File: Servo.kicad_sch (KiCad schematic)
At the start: 28 parts, among them J10 Conn_01x03_Pin, J11 Conn_01x03_Pin, J12 Conn_01x03_Pin, J13 Conn_01x03_Pin, J14 Conn_01x03_Pin, J15 Conn_01x03_Pin, J2 Conn_01x03_Pin, J3 Conn_01x03_Pin, J4 Conn_01x03_Pin, J5 Conn_01x03_Pin, J6 Conn_01x03_Pin, J7 Conn_01x03_Pin, J8 Conn_01x03_Pin, J9 Conn_01x03_Pin

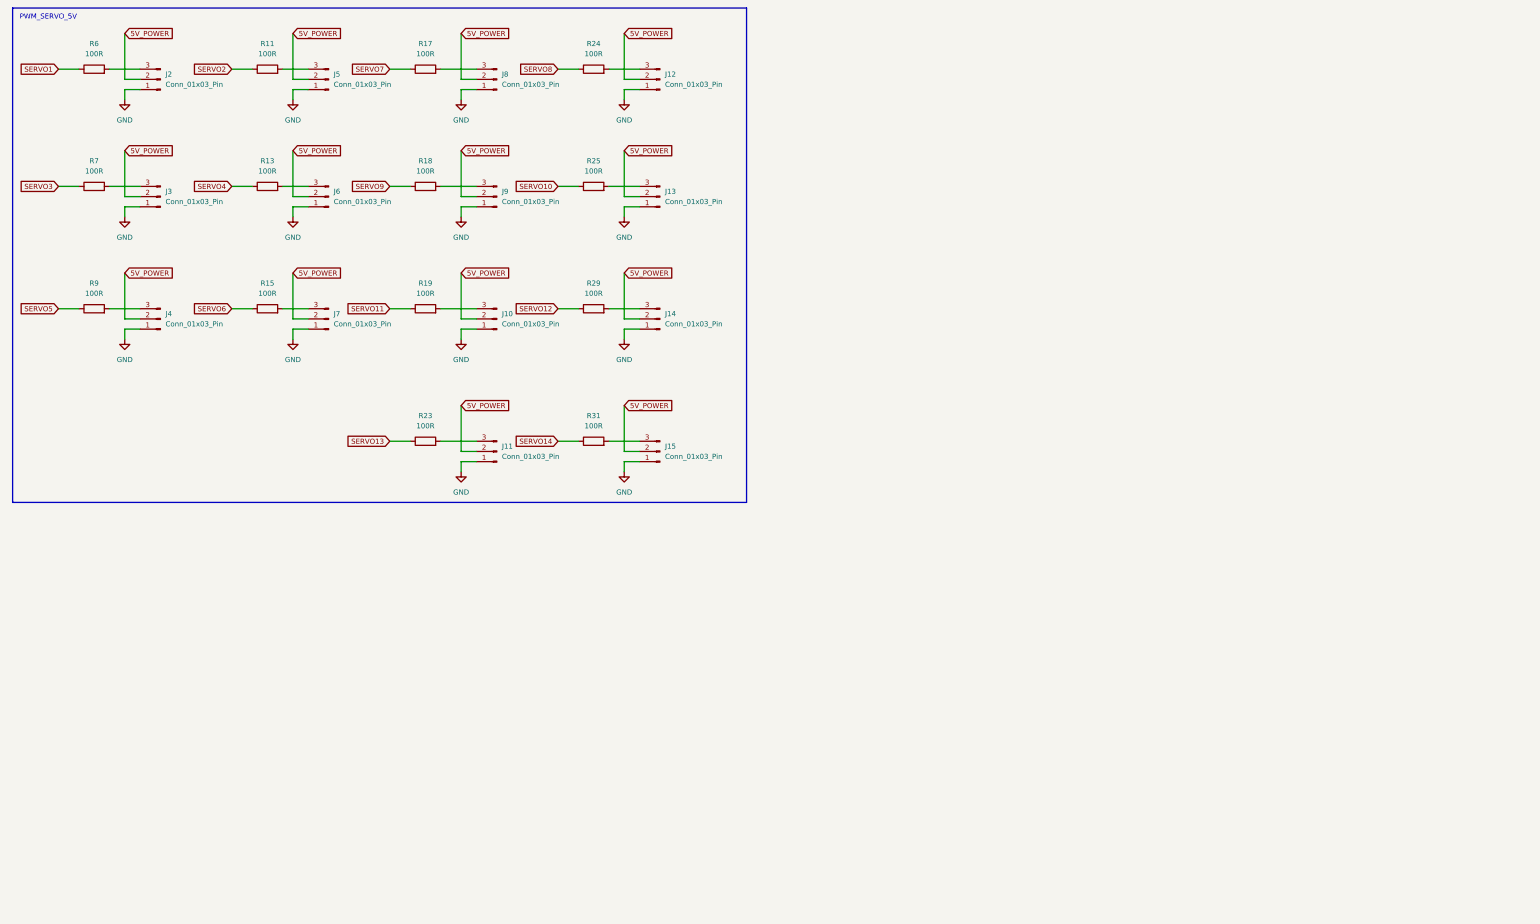
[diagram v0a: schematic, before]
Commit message: update servo output
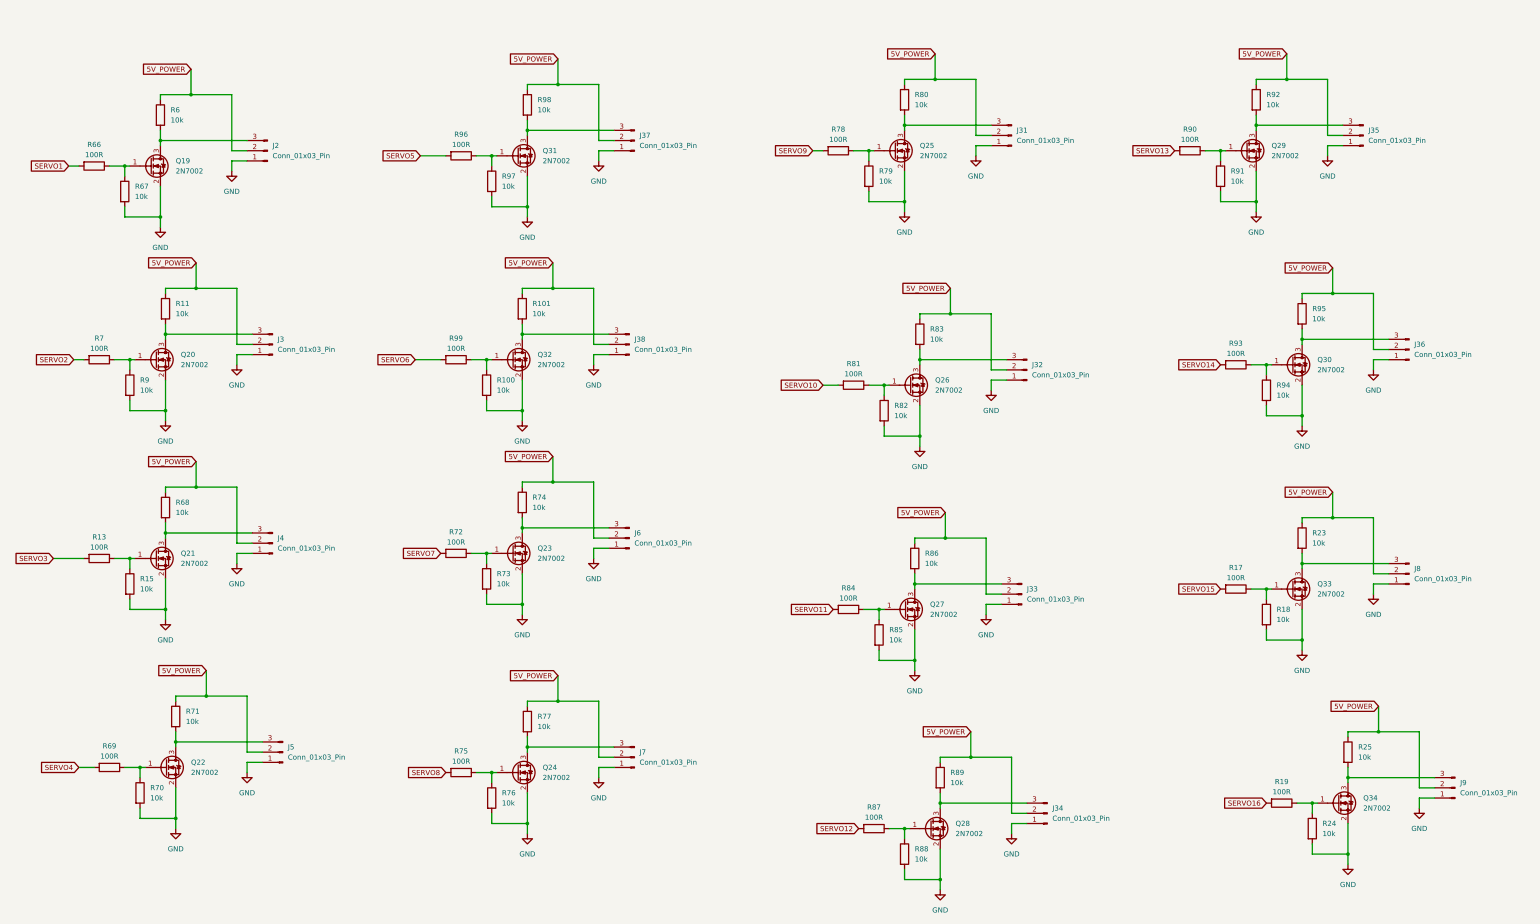
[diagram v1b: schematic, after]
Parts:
- removed J10, J11, J12, J13, J14, J15: Conn_01x03_Pin, symbol Connector:Conn_01x03_Pin
- removed R29, R31: 100R, symbol Device:R
- added J31, J32, J33, J34, J35, J36, J37, J38: Conn_01x03_Pin, Connector_JST:JST_XH_B3B-XH-AM_1x03_P2.50mm_Vertical, symbol Connector:Conn_01x03_Pin
- added Q19, Q20, Q21, Q22, Q23, Q24, Q25, Q26, Q27, Q28, Q29, Q30, Q31, Q32, Q33, Q34: 2N7002, Package_TO_SOT_SMD:SOT-23, symbol Transistor_FET:2N7002
- added R100, R101, R67, R68, R70, R71, R73, R74, R76, R77, R79, R80, R82, R83, R85, R86, R88, R89, R91, R92, R94, R95, R97, R98: 10k, Resistor_SMD:R_0201_0603Metric_Pad0.64x0.40mm_HandSolder, symbol Device:R
- added R66, R69, R72, R75, R78, R81, R84, R87, R90, R93, R96, R99: 100R, Resistor_SMD:R_0201_0603Metric_Pad0.64x0.40mm_HandSolder, symbol Device:R
- J2, J3, J4, J5, J6, J7, J8, J9: footprint (none) -> Connector_JST:JST_XH_B3B-XH-AM_1x03_P2.50mm_Vertical
- R11, R15, R18, R23, R24, R25, R6, R9: value 100R -> 10k; footprint (none) -> Resistor_SMD:R_0201_0603Metric_Pad0.64x0.40mm_HandSolder
- R13, R17, R19, R7: footprint (none) -> Resistor_SMD:R_0201_0603Metric_Pad0.64x0.40mm_HandSolder
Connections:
- net 5V_POWER: now also R11.1, R23.1, R25.1, R6.1, J31.2 (Pin_2), J32.2 (Pin_2), J33.2 (Pin_2), J34.2 (Pin_2), J35.2 (Pin_2), J36.2 (Pin_2), J37.2 (Pin_2), J38.2 (Pin_2), R101.1, R68.1, R71.1, R74.1, R77.1, R80.1, R83.1, R86.1, R89.1, R92.1, R95.1, R98.1
- net GND: now also R15.2, R18.2, R24.2, R9.2, J31.1 (Pin_1), J32.1 (Pin_1), J33.1 (Pin_1), J34.1 (Pin_1), J35.1 (Pin_1), J36.1 (Pin_1), J37.1 (Pin_1), J38.1 (Pin_1), Q19.2 (S), Q20.2 (S), Q21.2 (S), Q22.2 (S), Q23.2 (S), Q24.2 (S), Q25.2 (S), Q26.2 (S), Q27.2 (S), Q28.2 (S), Q29.2 (S), Q30.2 (S), Q31.2 (S), Q32.2 (S), Q33.2 (S), Q34.2 (S), R100.2, R67.2, R70.2, R73.2, R76.2, R79.2, R82.2, R85.2, R88.2, R91.2, R94.2, R97.2
- net SERVO1: now also R66.2; no longer R6.1
- net SERVO10: now also R81.2; no longer R25.1
- net SERVO11: now also R84.2; no longer R19.1
- net SERVO12: now also R87.2
- net SERVO13: now also R90.2; no longer R23.1
- net SERVO14: now also R93.2
- net SERVO2: now also R7.2; no longer R11.1
- net SERVO3: now also R13.2; no longer R7.1
- net SERVO4: now also R69.2; no longer R13.1
- net SERVO5: now also R96.2; no longer R9.1
- net SERVO6: now also R99.2; no longer R15.1
- net SERVO7: now also R72.2; no longer R17.1
- net SERVO8: now also R75.2; no longer R24.1
- net SERVO9: now also R78.2; no longer R18.1
- net at J9.3 (Pin_3): now also R25.2, Q34.3 (D); no longer R18.2
- net at J7.3 (Pin_3): now also Q24.3 (D), R77.2; no longer R15.2
- net at J3.3 (Pin_3): now also R11.2, Q20.3 (D); no longer R7.2
- net at J8.3 (Pin_3): now also R23.2, Q33.3 (D); no longer R17.2
- net at J6.3 (Pin_3): now also Q23.3 (D), R74.2; no longer R13.2
- net at J5.3 (Pin_3): now also Q22.3 (D), R71.2; no longer R11.2
- net at J2.3 (Pin_3), R6.2: now also Q19.3 (D)
- net at J4.3 (Pin_3): now also Q21.3 (D), R68.2; no longer R9.2
- net SERVO16: now reaches R19.2
- new net: Q20.1 (G), R7.1, R9.1
- new net: Q30.1 (G), R93.1, R94.1
- new net: J36.3 (Pin_3), Q30.3 (D), R95.2
- new net: Q26.1 (G), R81.1, R82.1
- new net: J32.3 (Pin_3), Q26.3 (D), R83.2
- new net: Q21.1 (G), R13.1, R15.1
- new net: Q33.1 (G), R17.1, R18.1
- new net: J33.3 (Pin_3), Q27.3 (D), R86.2
- new net: Q24.1 (G), R75.1, R76.1
- new net: Q23.1 (G), R72.1, R73.1
- new net: J34.3 (Pin_3), Q28.3 (D), R89.2
- new net: Q34.1 (G), R19.1, R24.1
- new net: Q25.1 (G), R78.1, R79.1
- new net: Q32.1 (G), R100.1, R99.1
- new net: Q19.1 (G), R66.1, R67.1
- new net: J35.3 (Pin_3), Q29.3 (D), R92.2
- new net: J31.3 (Pin_3), Q25.3 (D), R80.2
- new net: Q29.1 (G), R90.1, R91.1
- new net: Q31.1 (G), R96.1, R97.1
- new net: J37.3 (Pin_3), Q31.3 (D), R98.2
- new net: J38.3 (Pin_3), Q32.3 (D), R101.2
- new net: Q27.1 (G), R84.1, R85.1
- new net: Q22.1 (G), R69.1, R70.1
- new net: Q28.1 (G), R87.1, R88.1
- new net SERVO15: R17.2
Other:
- note removed: "PWM_SERVO_5V"
- moved on the sheet: J2

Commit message: v1 - need to change resistor package
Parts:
- R100, R101: footprint Resistor_SMD:R_0201_0603Metric_Pad0.64x0.40mm_HandSolder -> Capacitor_SMD:C_0402_1005Metric
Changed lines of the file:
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@@
 			)
 		)
-		(property "Footprint" "Resistor_SMD:R_0201_0603Metric_Pad0.64x0.40mm_HandSolder"
+		(property "Footprint" "Capacitor_SMD:C_0402_1005Metric"
 			(at 137.922 113.03 90)
 			(effects
@@
 			)
 		)
-		(property "Footprint" "Resistor_SMD:R_0201_0603Metric_Pad0.64x0.40mm_HandSolder"
+		(property "Footprint" "Capacitor_SMD:C_0402_1005Metric"
 			(at 146.812 93.98 90)
 			(effects

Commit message: fix resistor and add schematic in pdf
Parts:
- R11, R13, R15, R17, R18, R19, R23, R24, R25, R6, R66, R67, R68, R69, R7, R70, R71, R72, R73, R74, R75, R76, R77, R78, R79, R80, R81, R82, R83, R84, R85, R86, R87, R88, R89, R9, R90, R91, R92, R93, R94, R95, R96, R97, R98, R99: footprint Resistor_SMD:R_0201_0603Metric_Pad0.64x0.40mm_HandSolder -> Resistor_SMD:R_0402_1005Metric
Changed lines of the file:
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@@
 			)
 		)
-		(property "Footprint" "Resistor_SMD:R_0201_0603Metric_Pad0.64x0.40mm_HandSolder"
+		(property "Footprint" "Resistor_SMD:R_0402_1005Metric"
 			(at 49.022 113.03 90)
 			(effects
@@
 			)
 		)
-		(property "Footprint" "Resistor_SMD:R_0201_0603Metric_Pad0.64x0.40mm_HandSolder"
+		(property "Footprint" "Resistor_SMD:R_0402_1005Metric"
 			(at 245.872 100.33 90)
 			(effects
@@
 			)
 		)
-		(property "Footprint" "Resistor_SMD:R_0201_0603Metric_Pad0.64x0.40mm_HandSolder"
+		(property "Footprint" "Resistor_SMD:R_0402_1005Metric"
 			(at 43.18 154.432 90)
 			(effects
@@
 			)
 		)
-		(property "Footprint" "Resistor_SMD:R_0201_0603Metric_Pad0.64x0.40mm_HandSolder"
+		(property "Footprint" "Resistor_SMD:R_0402_1005Metric"
 			(at 332.232 170.18 90)
 			(effects
@@
 			)
 		)
-		(property "Footprint" "Resistor_SMD:R_0201_0603Metric_Pad0.64x0.40mm_HandSolder"
+		(property "Footprint" "Resistor_SMD:R_0402_1005Metric"
 			(at 139.192 215.9 90)
 			(effects
@@
 			)
 		)
-		(property "Footprint" "Resistor_SMD:R_0201_0603Metric_Pad0.64x0.40mm_HandSolder"
+		(property "Footprint" "Resistor_SMD:R_0402_1005Metric"
 			(at 133.35 207.772 90)
 			(effects
@@
 			)
 		)
-		(property "Footprint" "Resistor_SMD:R_0201_0603Metric_Pad0.64x0.40mm_HandSolder"
+		(property "Footprint" "Resistor_SMD:R_0402_1005Metric"
 			(at 49.022 162.56 90)
 			(effects
@@
 			)
 		)
-		(property "Footprint" "Resistor_SMD:R_0201_0603Metric_Pad0.64x0.40mm_HandSolder"
+		(property "Footprint" "Resistor_SMD:R_0402_1005Metric"
 			(at 250.952 210.82 90)
 			(effects
@@
 			)
 		)
-		(property "Footprint" "Resistor_SMD:R_0201_0603Metric_Pad0.64x0.40mm_HandSolder"
+		(property "Footprint" "Resistor_SMD:R_0402_1005Metric"
 			(at 148.082 196.85 90)
 			(effects
@@
 			)
 		)
-		(property "Footprint" "Resistor_SMD:R_0201_0603Metric_Pad0.64x0.40mm_HandSolder"
+		(property "Footprint" "Resistor_SMD:R_0402_1005Metric"
 			(at 326.39 106.172 90)
 			(effects
@@
 			)
 		)
-		(property "Footprint" "Resistor_SMD:R_0201_0603Metric_Pad0.64x0.40mm_HandSolder"
+		(property "Footprint" "Resistor_SMD:R_0402_1005Metric"
 			(at 227.33 52.832 90)
 			(effects
@@
 			)
 		)
-		(property "Footprint" "Resistor_SMD:R_0201_0603Metric_Pad0.64x0.40mm_HandSolder"
+		(property "Footprint" "Resistor_SMD:R_0402_1005Metric"
 			(at 341.122 151.13 90)
 			(effects
@@
 			)
 		)
-		(property "Footprint" "Resistor_SMD:R_0201_0603Metric_Pad0.64x0.40mm_HandSolder"
+		(property "Footprint" "Resistor_SMD:R_0402_1005Metric"
 			(at 47.752 64.77 90)
 			(effects
@@
 			)
 		)
-		(property "Footprint" "Resistor_SMD:R_0201_0603Metric_Pad0.64x0.40mm_HandSolder"
+		(property "Footprint" "Resistor_SMD:R_0402_1005Metric"
 			(at 329.692 41.91 90)
 			(effects
@@
 			)
 		)
-		(property "Footprint" "Resistor_SMD:R_0201_0603Metric_Pad0.64x0.40mm_HandSolder"
+		(property "Footprint" "Resistor_SMD:R_0402_1005Metric"
 			(at 56.642 45.72 90)
 			(effects
@@
 			)
 		)
-		(property "Footprint" "Resistor_SMD:R_0201_0603Metric_Pad0.64x0.40mm_HandSolder"
+		(property "Footprint" "Resistor_SMD:R_0402_1005Metric"
 			(at 146.812 142.24 90)
 			(effects
@@
 			)
 		)
-		(property "Footprint" "Resistor_SMD:R_0201_0603Metric_Pad0.64x0.40mm_HandSolder"
+		(property "Footprint" "Resistor_SMD:R_0402_1005Metric"
 			(at 242.062 41.91 90)
 			(effects
@@
 			)
 		)
-		(property "Footprint" "Resistor_SMD:R_0201_0603Metric_Pad0.64x0.40mm_HandSolder"
+		(property "Footprint" "Resistor_SMD:R_0402_1005Metric"
 			(at 57.912 93.98 90)
 			(effects
@@
 			)
 		)
-		(property "Footprint" "Resistor_SMD:R_0201_0603Metric_Pad0.64x0.40mm_HandSolder"
+		(property "Footprint" "Resistor_SMD:R_0402_1005Metric"
 			(at 314.96 52.832 90)
 			(effects
@@
 			)
 		)
-		(property "Footprint" "Resistor_SMD:R_0201_0603Metric_Pad0.64x0.40mm_HandSolder"
+		(property "Footprint" "Resistor_SMD:R_0402_1005Metric"
 			(at 233.172 60.96 90)
 			(effects
@@
 			)
 		)
-		(property "Footprint" "Resistor_SMD:R_0201_0603Metric_Pad0.64x0.40mm_HandSolder"
+		(property "Footprint" "Resistor_SMD:R_0402_1005Metric"
 			(at 137.922 161.29 90)
 			(effects
@@
 			)
 		)
-		(property "Footprint" "Resistor_SMD:R_0201_0603Metric_Pad0.64x0.40mm_HandSolder"
+		(property "Footprint" "Resistor_SMD:R_0402_1005Metric"
 			(at 231.14 111.252 90)
 			(effects
@@
 			)
 		)
-		(property "Footprint" "Resistor_SMD:R_0201_0603Metric_Pad0.64x0.40mm_HandSolder"
+		(property "Footprint" "Resistor_SMD:R_0402_1005Metric"
 			(at 320.802 60.96 90)
 			(effects
@@
 			)
 		)
-		(property "Footprint" "Resistor_SMD:R_0201_0603Metric_Pad0.64x0.40mm_HandSolder"
+		(property "Footprint" "Resistor_SMD:R_0402_1005Metric"
 			(at 229.87 167.132 90)
 			(effects
@@
 			)
 		)
-		(property "Footprint" "Resistor_SMD:R_0201_0603Metric_Pad0.64x0.40mm_HandSolder"
+		(property "Footprint" "Resistor_SMD:R_0402_1005Metric"
 			(at 132.08 153.162 90)
 			(effects
@@
 			)
 		)
-		(property "Footprint" "Resistor_SMD:R_0201_0603Metric_Pad0.64x0.40mm_HandSolder"
+		(property "Footprint" "Resistor_SMD:R_0402_1005Metric"
 			(at 51.562 214.63 90)
 			(effects
@@
 			)
 		)
-		(property "Footprint" "Resistor_SMD:R_0201_0603Metric_Pad0.64x0.40mm_HandSolder"
+		(property "Footprint" "Resistor_SMD:R_0402_1005Metric"
 			(at 235.712 175.26 90)
 			(effects
@@
 			)
 		)
-		(property "Footprint" "Resistor_SMD:R_0201_0603Metric_Pad0.64x0.40mm_HandSolder"
+		(property "Footprint" "Resistor_SMD:R_0402_1005Metric"
 			(at 132.08 104.902 90)
 			(effects
@@
 			)
 		)
-		(property "Footprint" "Resistor_SMD:R_0201_0603Metric_Pad0.64x0.40mm_HandSolder"
+		(property "Footprint" "Resistor_SMD:R_0402_1005Metric"
 			(at 244.602 156.21 90)
 			(effects
@@
 			)
 		)
-		(property "Footprint" "Resistor_SMD:R_0201_0603Metric_Pad0.64x0.40mm_HandSolder"
+		(property "Footprint" "Resistor_SMD:R_0402_1005Metric"
 			(at 332.232 114.3 90)
 			(effects
@@
 			)
 		)
-		(property "Footprint" "Resistor_SMD:R_0201_0603Metric_Pad0.64x0.40mm_HandSolder"
+		(property "Footprint" "Resistor_SMD:R_0402_1005Metric"
 			(at 43.18 104.902 90)
 			(effects
@@
 			)
 		)
-		(property "Footprint" "Resistor_SMD:R_0201_0603Metric_Pad0.64x0.40mm_HandSolder"
+		(property "Footprint" "Resistor_SMD:R_0402_1005Metric"
 			(at 133.35 54.102 90)
 			(effects
@@
 			)
 		)
-		(property "Footprint" "Resistor_SMD:R_0201_0603Metric_Pad0.64x0.40mm_HandSolder"
+		(property "Footprint" "Resistor_SMD:R_0402_1005Metric"
 			(at 242.062 229.87 90)
 			(effects
@@
 			)
 		)
-		(property "Footprint" "Resistor_SMD:R_0201_0603Metric_Pad0.64x0.40mm_HandSolder"
+		(property "Footprint" "Resistor_SMD:R_0402_1005Metric"
 			(at 60.452 195.58 90)
 			(effects
@@
 			)
 		)
-		(property "Footprint" "Resistor_SMD:R_0201_0603Metric_Pad0.64x0.40mm_HandSolder"
+		(property "Footprint" "Resistor_SMD:R_0402_1005Metric"
 			(at 352.552 204.47 90)
 			(effects
@@
 			)
 		)
-		(property "Footprint" "Resistor_SMD:R_0201_0603Metric_Pad0.64x0.40mm_HandSolder"
+		(property "Footprint" "Resistor_SMD:R_0402_1005Metric"
 			(at 341.122 95.25 90)
 			(effects
@@
 			)
 		)
-		(property "Footprint" "Resistor_SMD:R_0201_0603Metric_Pad0.64x0.40mm_HandSolder"
+		(property "Footprint" "Resistor_SMD:R_0402_1005Metric"
 			(at 45.72 206.502 90)
 			(effects
@@
 			)
 		)
-		(property "Footprint" "Resistor_SMD:R_0201_0603Metric_Pad0.64x0.40mm_HandSolder"
+		(property "Footprint" "Resistor_SMD:R_0402_1005Metric"
 			(at 236.982 119.38 90)
 			(effects
@@
 			)
 		)
-		(property "Footprint" "Resistor_SMD:R_0201_0603Metric_Pad0.64x0.40mm_HandSolder"
+		(property "Footprint" "Resistor_SMD:R_0402_1005Metric"
 			(at 41.91 56.642 90)
 			(effects
@@
 			)
 		)
-		(property "Footprint" "Resistor_SMD:R_0201_0603Metric_Pad0.64x0.40mm_HandSolder"
+		(property "Footprint" "Resistor_SMD:R_0402_1005Metric"
 			(at 337.82 215.392 90)
 			(effects
@@
 			)
 		)
-		(property "Footprint" "Resistor_SMD:R_0201_0603Metric_Pad0.64x0.40mm_HandSolder"
+		(property "Footprint" "Resistor_SMD:R_0402_1005Metric"
 			(at 343.662 223.52 90)
 			(effects
@@
 			)
 		)
-		(property "Footprint" "Resistor_SMD:R_0201_0603Metric_Pad0.64x0.40mm_HandSolder"
+		(property "Footprint" "Resistor_SMD:R_0402_1005Metric"
 			(at 148.082 43.18 90)
 			(effects
@@
 			)
 		)
-		(property "Footprint" "Resistor_SMD:R_0201_0603Metric_Pad0.64x0.40mm_HandSolder"
+		(property "Footprint" "Resistor_SMD:R_0402_1005Metric"
 			(at 236.22 221.742 90)
 			(effects
@@
 			)
 		)
-		(property "Footprint" "Resistor_SMD:R_0201_0603Metric_Pad0.64x0.40mm_HandSolder"
+		(property "Footprint" "Resistor_SMD:R_0402_1005Metric"
 			(at 326.39 162.052 90)
 			(effects
@@
 			)
 		)
-		(property "Footprint" "Resistor_SMD:R_0201_0603Metric_Pad0.64x0.40mm_HandSolder"
+		(property "Footprint" "Resistor_SMD:R_0402_1005Metric"
 			(at 57.912 143.51 90)
 			(effects
@@
 			)
 		)
-		(property "Footprint" "Resistor_SMD:R_0201_0603Metric_Pad0.64x0.40mm_HandSolder"
+		(property "Footprint" "Resistor_SMD:R_0402_1005Metric"
 			(at 139.192 62.23 90)
 			(effects
